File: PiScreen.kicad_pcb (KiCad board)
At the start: 2 copper layers, 56 x 36.5 mm, 113 parts, among them P1 M02X05, P2 M02X05, P3 CONN_14, P4 CONN_5, P5 CONN_5, P6 CONN_5

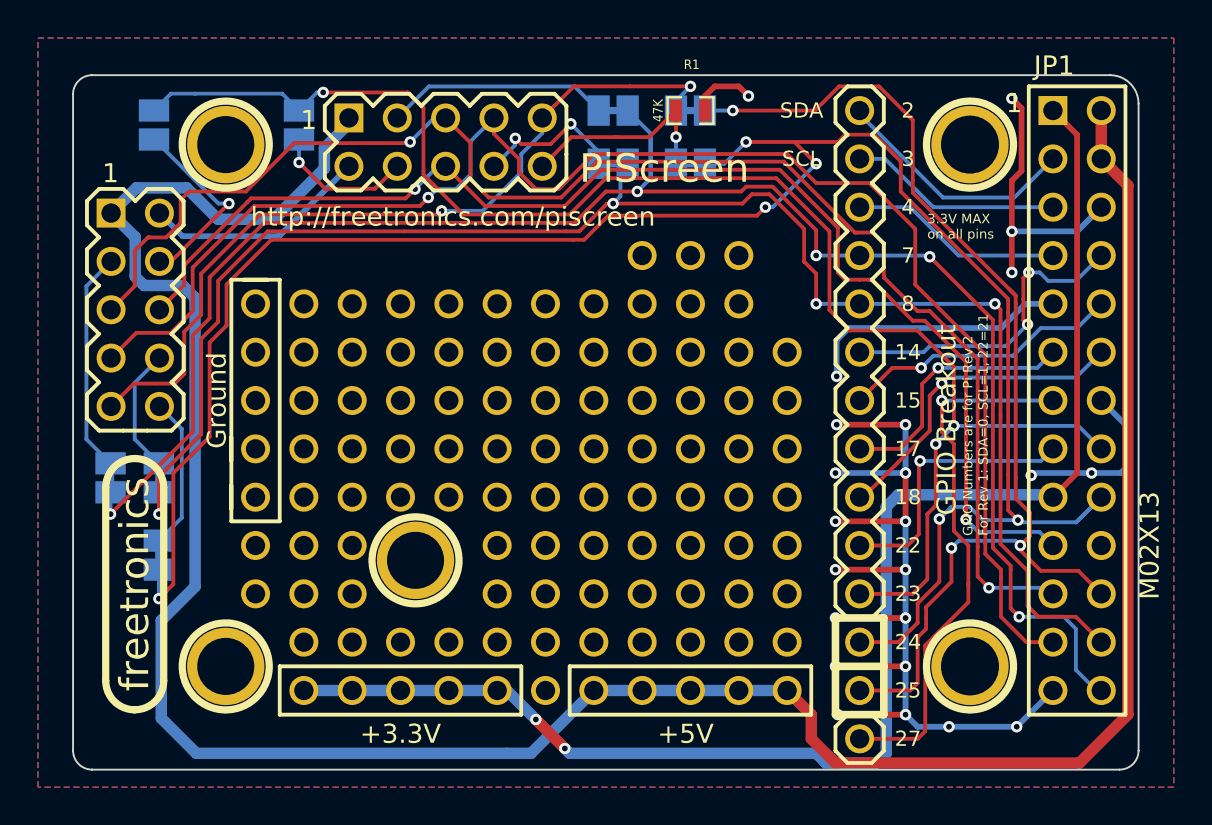
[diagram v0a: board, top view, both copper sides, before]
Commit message: Increase silkscreen font sizes
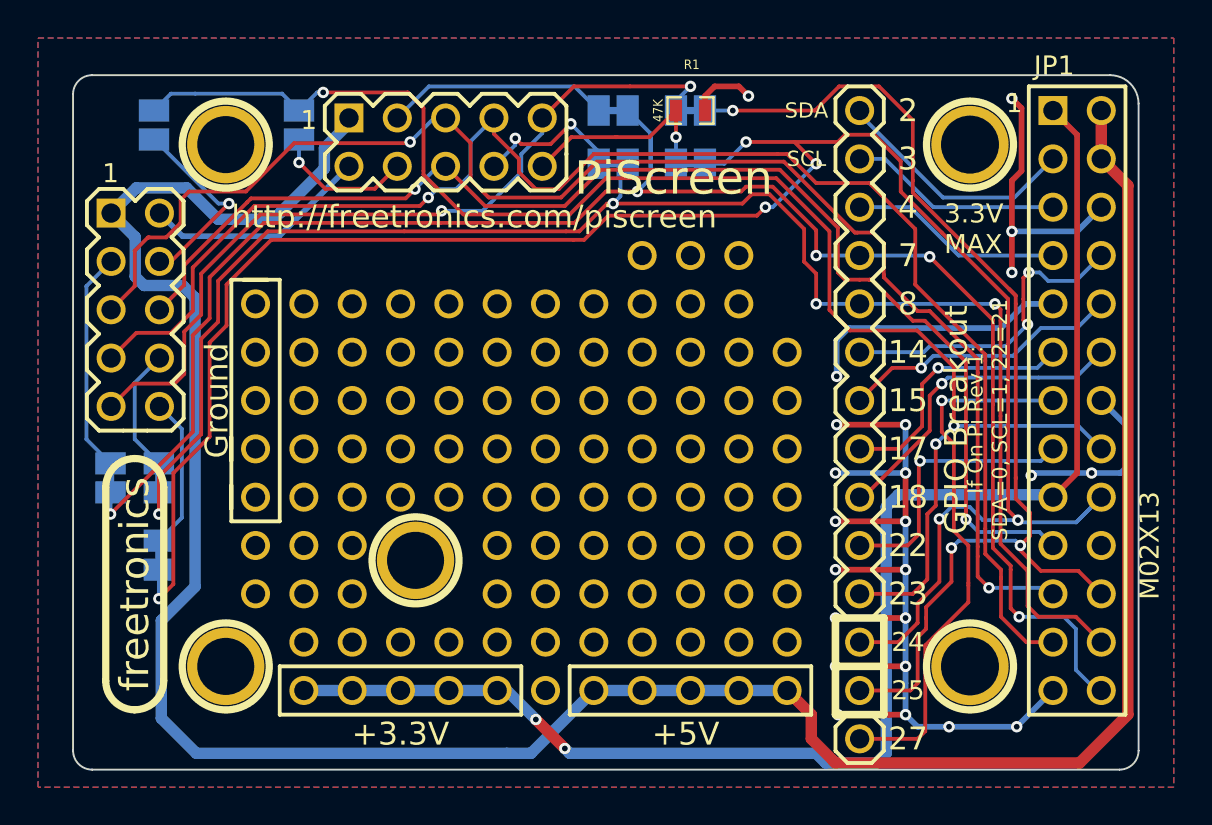
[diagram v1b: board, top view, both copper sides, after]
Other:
- board text added: "3.3V MAX"
- board text added: "Designed by Angus Gratton (c) 2013 Freetronics Pty Ltd TAPR Open Hardware License"
- board text added: "If On Pi Rev 1: SDA=0, SCL=1, 22=21"
- board text added: "V1.0 SKU: PISC"
- board text removed: "3.3V MAX on all pins"
- board text removed: "Designed by Angus Gratton (c) 2013 Freetronics Pty Ltd TAPR Open Hardware License v0.1 SKU: PISC"
- board text removed: "GPIO Numbers are for Pi Rev 2 For Rev 1: SDA=0, SCL=1, 22=21"
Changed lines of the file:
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@@
     (links 66)
     (no_connects 0)
-    (area 137.16 81.812 199.581231 124.643066)
+    (area 137.16 81.812 196.850001 124.643066)
     (thickness 1.6)
-    (drawings 85)
+    (drawings 86)
     (tracks 563)
     (zones 0)
@@
     (18 B.Paste user)
     (19 F.Paste user)
-    (20 B.SilkS user hide)
+    (20 B.SilkS user)
     (21 F.SilkS user)
     (22 B.Mask user)
@@
     (fp_arc (start -5.08 0) (end -6.604 0) (angle -90) (layer B.SilkS) (width 0.381))
   )
+  (gr_text "V1.0\nSKU: PISC" (at 176.53 91.313 90) (layer B.SilkS)
+    (effects (font (size 0.8 0.8) (thickness 0.15)) (justify left mirror))
+  )
   (gr_text P1 (at 153.7335 83.312) (layer Cmts.User)
     (effects (font (size 1.5 1.5) (thickness 0.3)))
@@
     (effects (font (size 0.8 0.8) (thickness 0.175)) (justify mirror))
   )
-  (gr_text SCL (at 177.292 88.9) (layer F.SilkS)
+  (gr_text SCL (at 177.546 88.9) (layer F.SilkS)
     (effects (font (size 0.8 0.8) (thickness 0.175)))
   )
@@
     (effects (font (size 0.8 0.8) (thickness 0.175)) (justify mirror))
   )
-  (gr_text SDA (at 177.292 86.36) (layer F.SilkS)
+  (gr_text SDA (at 177.546 86.36) (layer F.SilkS)
     (effects (font (size 0.8 0.8) (thickness 0.175)))
   )
-  (gr_text "3.3V MAX\non all pins" (at 187.96 92.456) (layer B.SilkS)
-    (effects (font (size 0.5 0.5) (thickness 0.1)) (justify left mirror))
-  )
-  (gr_text "3.3V MAX\non all pins" (at 183.896 92.456) (layer F.SilkS)
-    (effects (font (size 0.5 0.5) (thickness 0.1)) (justify left))
-  )
-  (gr_text "Designed by Angus Gratton\n(c) 2013 Freetronics Pty Ltd\nTAPR Open Hardware License\n\nv0.1 SKU: PISC" (at 164.846 91.567) (layer B.SilkS)
-    (effects (font (size 0.5 0.5) (thickness 0.1)) (justify left mirror))
+  (gr_text "3.3V\nMAX\n" (at 187.833 92.583) (layer B.SilkS)
+    (effects (font (size 1 1) (thickness 0.2)) (justify left mirror))
+  )
+  (gr_text "3.3V\nMAX\n" (at 184.785 92.583) (layer F.SilkS)
+    (effects (font (size 1 1) (thickness 0.2)) (justify left))
+  )
+  (gr_text "Designed by Angus Gratton\n(c) 2013 Freetronics Pty Ltd\nTAPR Open Hardware License" (at 164.846 91.567) (layer B.SilkS)
+    (effects (font (size 0.8 0.8) (thickness 0.15)) (justify left mirror))
   )
   (gr_text 1 (at 140.97 89.662) (layer F.SilkS)
@@
   (gr_line (start 181.61 113.03) (end 181.61 115.57) (angle 90) (layer F.SilkS) (width 0.4))
   (gr_line (start 179.07 113.03) (end 181.61 113.03) (angle 90) (layer F.SilkS) (width 0.4))
-  (gr_text "GPIO Numbers are for Pi Rev 2\nFor Rev 1: SDA=0, SCL=1, 22=21" (at 186.436 108.712 90) (layer F.SilkS)
-    (effects (font (size 0.5 0.5) (thickness 0.1)) (justify left))
+  (gr_text "If On Pi Rev 1:\nSDA=0, SCL=1, 22=21" (at 187.071 102.616 90) (layer F.SilkS)
+    (effects (font (size 0.8 0.8) (thickness 0.15)))
   )
   (gr_text 27 (at 182.88 119.38) (layer B.SilkS)
-    (effects (font (size 0.8 0.8) (thickness 0.175)) (justify mirror))
+    (effects (font (size 1.2 1.2) (thickness 0.25)) (justify mirror))
   )
   (gr_text 27 (at 182.88 119.38) (layer F.SilkS)
-    (effects (font (size 0.8 0.8) (thickness 0.175)))
+    (effects (font (size 1.2 1.2) (thickness 0.25)))
   )
   (gr_text 25 (at 182.88 116.84) (layer F.SilkS)
-    (effects (font (size 0.8 0.8) (thickness 0.175)))
+    (effects (font (size 1 1) (thickness 0.2)))
   )
   (gr_text 25 (at 182.88 116.84) (layer B.SilkS)
-    (effects (font (size 0.8 0.8) (thickness 0.175)) (justify mirror))
+    (effects (font (size 1 1) (thickness 0.2)) (justify mirror))
   )
   (gr_text 24 (at 182.88 114.3) (layer B.SilkS)
-    (effects (font (size 0.8 0.8) (thickness 0.175)) (justify mirror))
+    (effects (font (size 1 1) (thickness 0.2)) (justify mirror))
   )
   (gr_text 24 (at 182.88 114.3) (layer F.SilkS)
-    (effects (font (size 0.8 0.8) (thickness 0.175)))
+    (effects (font (size 1 1) (thickness 0.2)))
   )
   (gr_text 23 (at 182.88 111.76) (layer B.SilkS)
-    (effects (font (size 0.8 0.8) (thickness 0.175)) (justify mirror))
+    (effects (font (size 1.2 1.2) (thickness 0.25)) (justify mirror))
   )
   (gr_text 23 (at 182.88 111.76) (layer F.SilkS)
-    (effects (font (size 0.8 0.8) (thickness 0.175)))
+    (effects (font (size 1.2 1.2) (thickness 0.25)))
   )
   (gr_text 22 (at 182.88 109.22) (layer B.SilkS)
-    (effects (font (size 0.8 0.8) (thickness 0.175)) (justify mirror))
+    (effects (font (size 1.2 1.2) (thickness 0.25)) (justify mirror))
   )
   (gr_text 22 (at 182.88 109.22) (layer F.SilkS)
-    (effects (font (size 0.8 0.8) (thickness 0.175)))
+    (effects (font (size 1.2 1.2) (thickness 0.25)))
   )
   (gr_text 18 (at 182.88 106.68) (layer B.SilkS)
-    (effects (font (size 0.8 0.8) (thickness 0.175)) (justify mirror))
+    (effects (font (size 1.2 1.2) (thickness 0.25)) (justify mirror))
   )
   (gr_text 18 (at 182.88 106.68) (layer F.SilkS)
-    (effects (font (size 0.8 0.8) (thickness 0.175)))
+    (effects (font (size 1.2 1.2) (thickness 0.25)))
   )
   (gr_text 17 (at 182.88 104.14) (layer B.SilkS)
-    (effects (font (size 0.8 0.8) (thickness 0.175)) (justify mirror))
+    (effects (font (size 1.2 1.2) (thickness 0.25)) (justify mirror))
   )
   (gr_text 17 (at 182.88 104.14) (layer F.SilkS)
-    (effects (font (size 0.8 0.8) (thickness 0.175)))
+    (effects (font (size 1.2 1.2) (thickness 0.25)))
   )
   (gr_text 15 (at 182.88 101.6) (layer B.SilkS)
-    (effects (font (size 0.8 0.8) (thickness 0.175)) (justify mirror))
+    (effects (font (size 1.2 1.2) (thickness 0.25)) (justify mirror))
   )
   (gr_text 15 (at 182.88 101.6) (layer F.SilkS)
-    (effects (font (size 0.8 0.8) (thickness 0.175)))
+    (effects (font (size 1.2 1.2) (thickness 0.25)))
   )
   (gr_text 14 (at 182.88 99.06) (layer B.SilkS)
-    (effects (font (size 0.8 0.8) (thickness 0.175)) (justify mirror))
+    (effects (font (size 1.2 1.2) (thickness 0.25)) (justify mirror))
   )
   (gr_text 14 (at 182.88 99.06) (layer F.SilkS)
-    (effects (font (size 0.8 0.8) (thickness 0.175)))
+    (effects (font (size 1.2 1.2) (thickness 0.25)))
   )
   (gr_text 8 (at 182.88 96.52) (layer B.SilkS)
-    (effects (font (size 0.8 0.8) (thickness 0.175)) (justify mirror))
+    (effects (font (size 1.2 1.2) (thickness 0.25)) (justify mirror))
   )
   (gr_text 8 (at 182.88 96.52) (layer F.SilkS)
-    (effects (font (size 0.8 0.8) (thickness 0.175)))
+    (effects (font (size 1.2 1.2) (thickness 0.25)))
   )
   (gr_text 7 (at 182.88 93.98) (layer B.SilkS)
-    (effects (font (size 0.8 0.8) (thickness 0.175)) (justify mirror))
+    (effects (font (size 1.2 1.2) (thickness 0.25)) (justify mirror))
   )
   (gr_text 7 (at 182.88 93.98) (layer F.SilkS)
-    (effects (font (size 0.8 0.8) (thickness 0.175)))
+    (effects (font (size 1.2 1.2) (thickness 0.25)))
   )
   (gr_text 4 (at 182.88 91.44) (layer B.SilkS)
-    (effects (font (size 0.8 0.8) (thickness 0.175)) (justify mirror))
+    (effects (font (size 1.2 1.2) (thickness 0.25)) (justify mirror))
   )
   (gr_text 4 (at 182.88 91.44) (layer F.SilkS)
-    (effects (font (size 0.8 0.8) (thickness 0.175)))
+    (effects (font (size 1.2 1.2) (thickness 0.25)))
   )
   (gr_text 3 (at 182.88 88.9) (layer B.SilkS)
-    (effects (font (size 0.8 0.8) (thickness 0.175)) (justify mirror))
+    (effects (font (size 1.2 1.2) (thickness 0.25)) (justify mirror))
   )
   (gr_text 3 (at 182.88 88.9) (layer F.SilkS)
-    (effects (font (size 0.8 0.8) (thickness 0.175)))
+    (effects (font (size 1.2 1.2) (thickness 0.25)))
   )
   (gr_text 2 (at 182.88 86.36) (layer B.SilkS)
-    (effects (font (size 0.8 0.8) (thickness 0.175)) (justify mirror))
+    (effects (font (size 1.2 1.2) (thickness 0.25)) (justify mirror))
   )
   (gr_text 2 (at 182.88 86.36) (layer F.SilkS)
-    (effects (font (size 0.8 0.8) (thickness 0.175)))
-  )
-  (gr_text "GPIO Breakout" (at 184.912 102.616 90) (layer F.SilkS)
-    (effects (font (size 1 1) (thickness 0.2)))
-  )
-  (gr_text "http://freetronics.com/piscreen\n" (at 148.336 91.948) (layer F.SilkS)
-    (effects (font (size 1 1) (thickness 0.2)) (justify left))
-  )
-  (gr_text PiScreen (at 165.608 89.408) (layer F.SilkS)
-    (effects (font (size 1.5 1.5) (thickness 0.3)) (justify left))
+    (effects (font (size 1.2 1.2) (thickness 0.25)))
+  )
+  (gr_text "GPIO Breakout" (at 185.42 102.616 90) (layer F.SilkS)
+    (effects (font (size 1.2 1.2) (thickness 0.25)))
+  )
+  (gr_text "http://freetronics.com/piscreen\n" (at 147.32 91.948) (layer F.SilkS)
+    (effects (font (size 1.2 1.2) (thickness 0.25)) (justify left))
+  )
+  (gr_text PiScreen (at 165.354 89.916) (layer F.SilkS)
+    (effects (font (size 1.75 1.75) (thickness 0.4)) (justify left))
   )
   (gr_text +5V (at 171.196 119.126) (layer B.SilkS)
-    (effects (font (size 1 1) (thickness 0.2)) (justify mirror))
+    (effects (font (size 1.2 1.2) (thickness 0.25)) (justify mirror))
   )
   (gr_text +5V (at 171.196 119.126) (layer F.SilkS)
-    (effects (font (size 1 1) (thickness 0.2)))
+    (effects (font (size 1.2 1.2) (thickness 0.25)))
   )
   (gr_text +3.3V (at 156.464 119.126) (layer B.SilkS)
-    (effects (font (size 1 1) (thickness 0.2)) (justify mirror))
+    (effects (font (size 1.2 1.2) (thickness 0.25)) (justify mirror))
   )
   (gr_text +3.3V (at 156.21 119.126) (layer F.SilkS)
-    (effects (font (size 1 1) (thickness 0.2)))
+    (effects (font (size 1.2 1.2) (thickness 0.25)))
   )
   (gr_text Ground (at 146.558 101.6 90) (layer B.SilkS)
-    (effects (font (size 1 1) (thickness 0.2)) (justify mirror))
+    (effects (font (size 1.2 1.2) (thickness 0.25)) (justify mirror))
   )
   (gr_text Ground (at 146.558 101.6 90) (layer F.SilkS)
-    (effects (font (size 1 1) (thickness 0.2)))
+    (effects (font (size 1.2 1.2) (thickness 0.25)))
   )
   (gr_line (start 140 121) (end 194 121) (angle 90) (layer Edge.Cuts) (width 0.1))

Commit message: PCB layout tweaks for v1.0
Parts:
- removed the 1pin_prototyping at (168.9, 94.0)
- removed the 1pin_prototyping at (171.4, 94.0)
- removed the 1pin_prototyping at (174.0, 94.0)
- added 1pin_prototyping: val**, 1pin_prototyping, F.Cu at (176.5, 96.5)
- moved R1 3.72 mm to (172.2, 90.0)
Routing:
- net GND: track 103.1 -> 128.5 mm, vias 23 -> 28
- net /GPIO24: track 108.6 -> 104.2 mm, vias 6 -> 5
- net /MOSI: track 66.9 -> 64.0 mm
- net /GPIO23: track 79.0 -> 76.2 mm
- net /MISO: track 76.3 -> 74.7 mm
- net /OLED_~CS: track 8.12 -> 6.87 mm
- net /GPIO7_CE1: track 93.3 -> 92.3 mm
- net /SCK: track 80.2 -> 79.3 mm
- net /OLED_~RST: track 11.1 -> 11.9 mm
- net /GPIO8_CE0: track 85.4 -> 86.0 mm
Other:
- board text added: "SJ5 / SJ8 SJ3 / SJ6"
- board text added: "SJ7 / SJ9 SJ4"
- board text removed: "Solder Jumpers SJ5 / SJ8 SJ3 / SJ6"
- board text removed: "Solder Jumpers SJ7 / SJ9 SJ4"

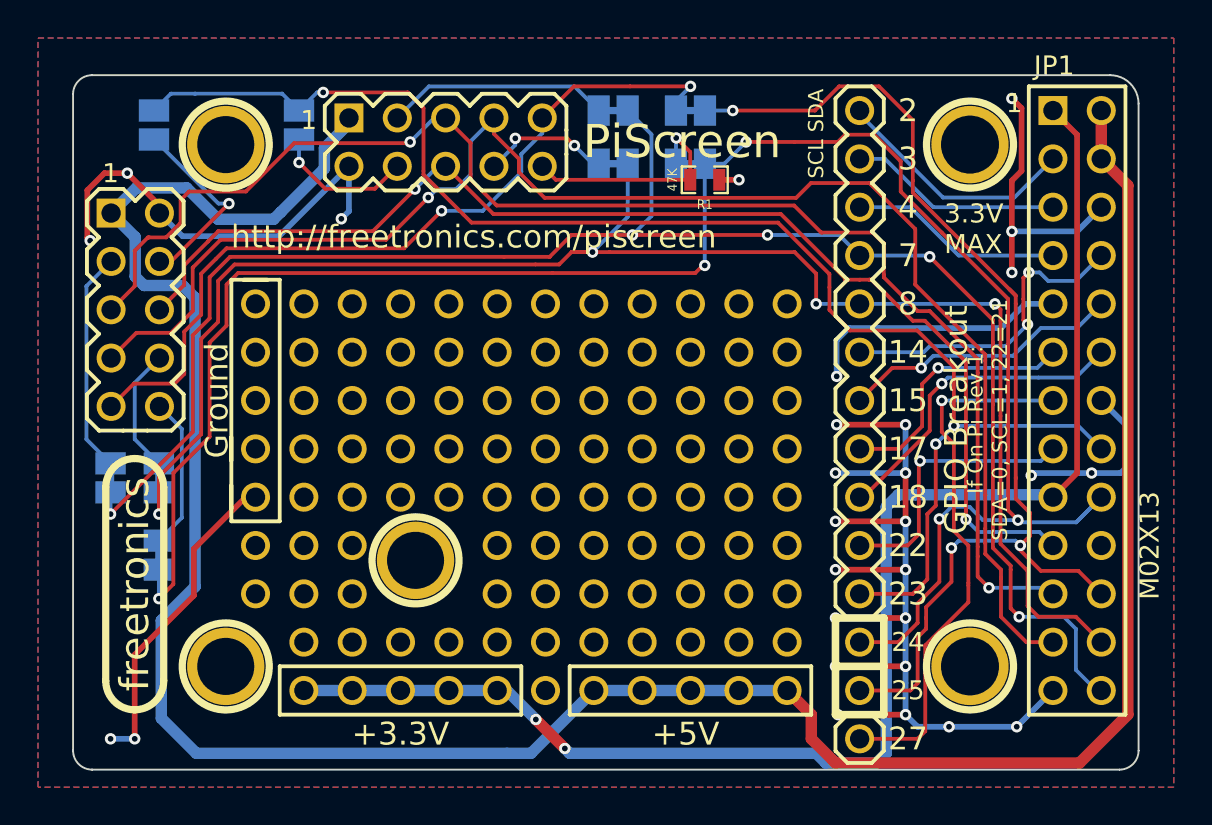
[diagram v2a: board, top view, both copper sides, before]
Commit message: Grow/simplify some silkscreen labels, improve grounding, bump to V1.1
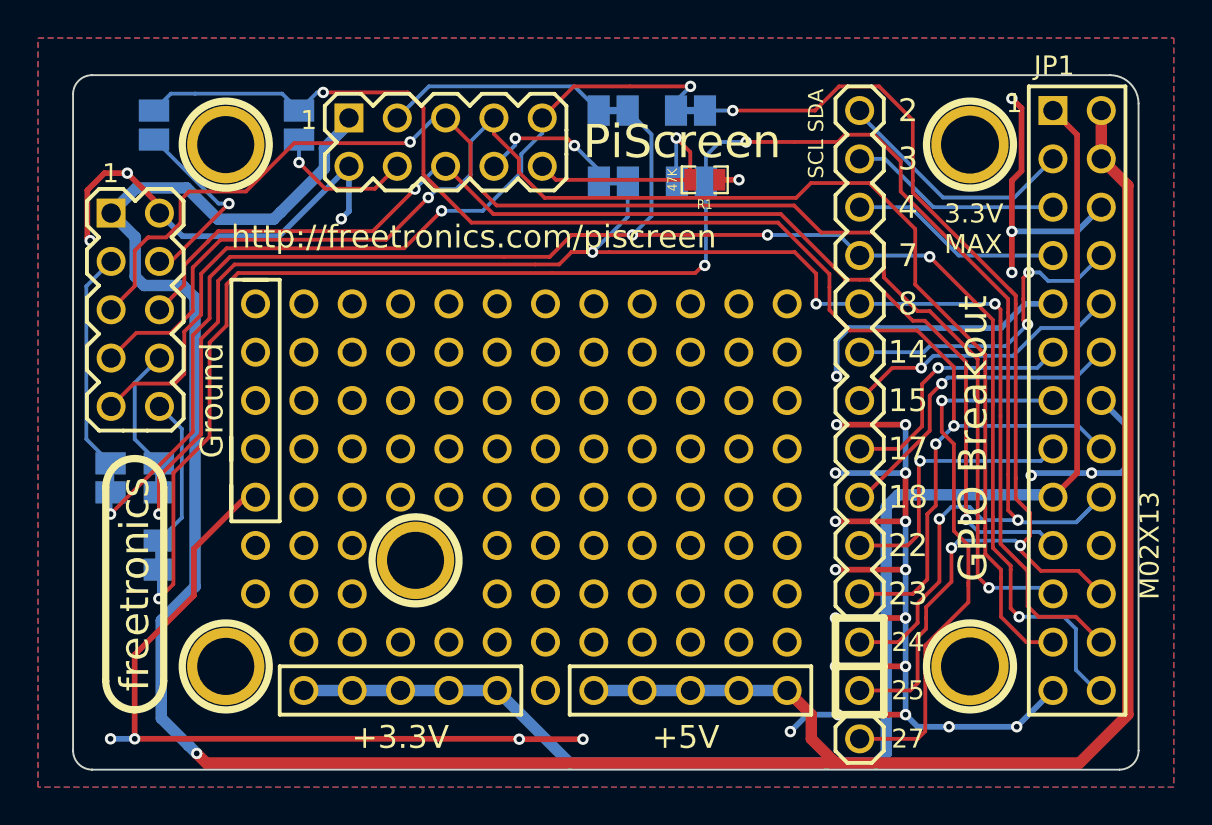
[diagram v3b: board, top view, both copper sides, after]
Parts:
- moved SJ3 0.95 mm to (171.5, 90.1)
- moved SJ6 0.95 mm to (167.4, 90.1)
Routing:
- net GND: track 128.5 -> 154.9 mm, vias 28 -> 31
- net +5V: track 141.0 -> 152.5 mm, vias 0 -> 1
- net /OLED_~RST: track 11.9 -> 12.9 mm
- net /GPIO8_CE0: track 86.0 -> 85.0 mm
- net /OLED_~CS: track 6.87 -> 7.63 mm
- net +3.3V: vias 2 -> 0
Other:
- board text added: "SJ3"
- board text added: "SJ5"
- board text added: "SJ6"
- board text added: "SJ8"
- board text added: "V1.1 SKU: PISC"
- board text removed: "If On Pi Rev 1: SDA=0, SCL=1, 22=21"
- board text removed: "SJ5 / SJ8 SJ3 / SJ6"
- board text removed: "V1.0 SKU: PISC"

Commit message: More silkscreen, grounding
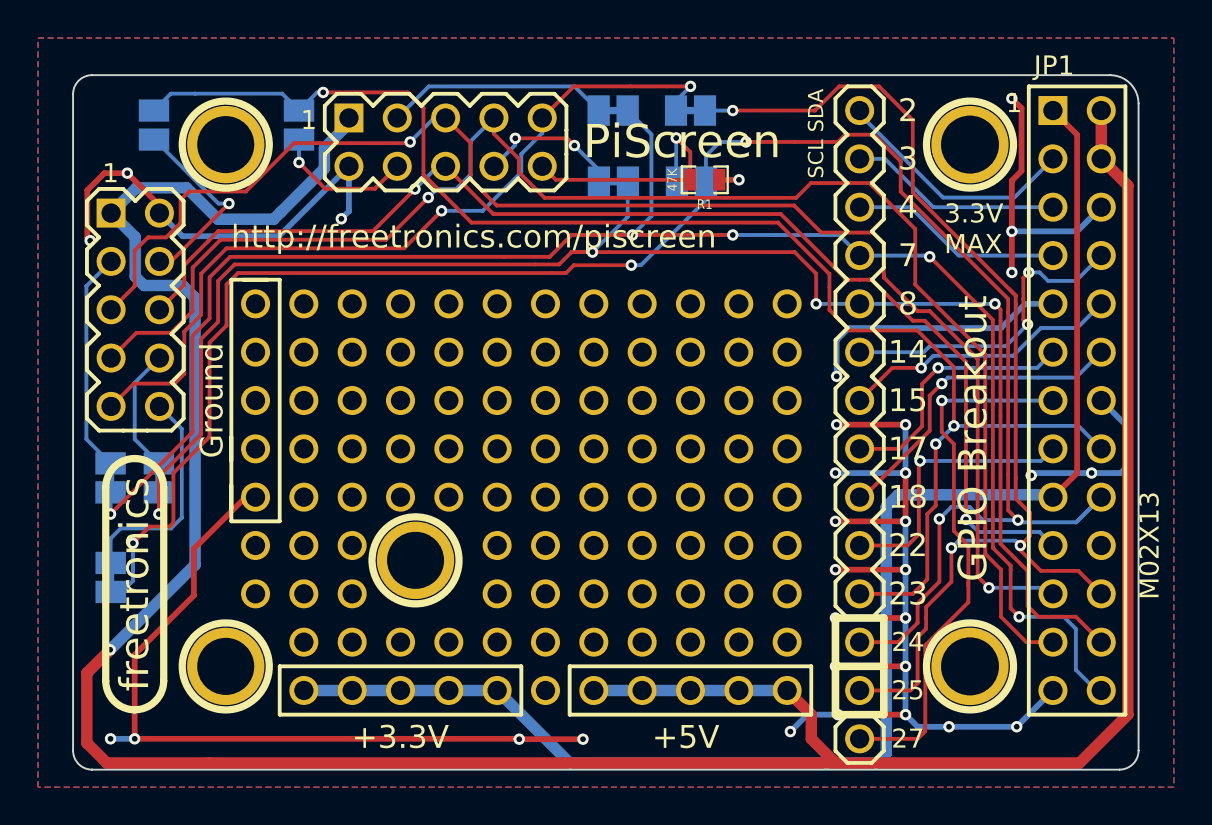
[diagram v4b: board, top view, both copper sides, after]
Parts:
- moved SJ4 2.79 mm to (141.0, 110.9)
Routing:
- net +5V: track 152.5 -> 158.8 mm
- net /OLED2_~RST: track 8.04 -> 11.8 mm
- net /GPIO24: track 104.5 -> 102.6 mm
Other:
- board text added: "SJ4"
- board text added: "SJ7"
- board text added: "SJ9"
- board text removed: "SJ7 / SJ9 SJ4"

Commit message: Fix SJ8 & SJ9 to be open by default (screen connecting to SPI CE0 not CE1)
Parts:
- SJ8, SJ9: footprint SJ_SHORTED -> SJ_OPEN
